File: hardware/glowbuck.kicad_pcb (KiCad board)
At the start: 4 copper layers, 80 x 50 mm, 130 parts, among them J101 Conn_02x08_Odd_Even, J102 Conn_01x04_Socket, J103 Conn_01x01_Pin, J104 Conn_01x01_Pin, J105 Conn_01x01_Pin, J201 USB_C_Receptacle_USB2.0_16P, J202 USB_C_Receptacle_USB2.0_16P, Q401 2N7002NXAKR, SW101 SW_Push, SW102 SW_Push, U101 ESP32-S3-WROOM-1, U102 INA181A3, U103 SN74LVC1T45DBV, U201 TPS25730D, U202 TPD2E2U06DCK, U301 AP63203WU, U401 SIC437A

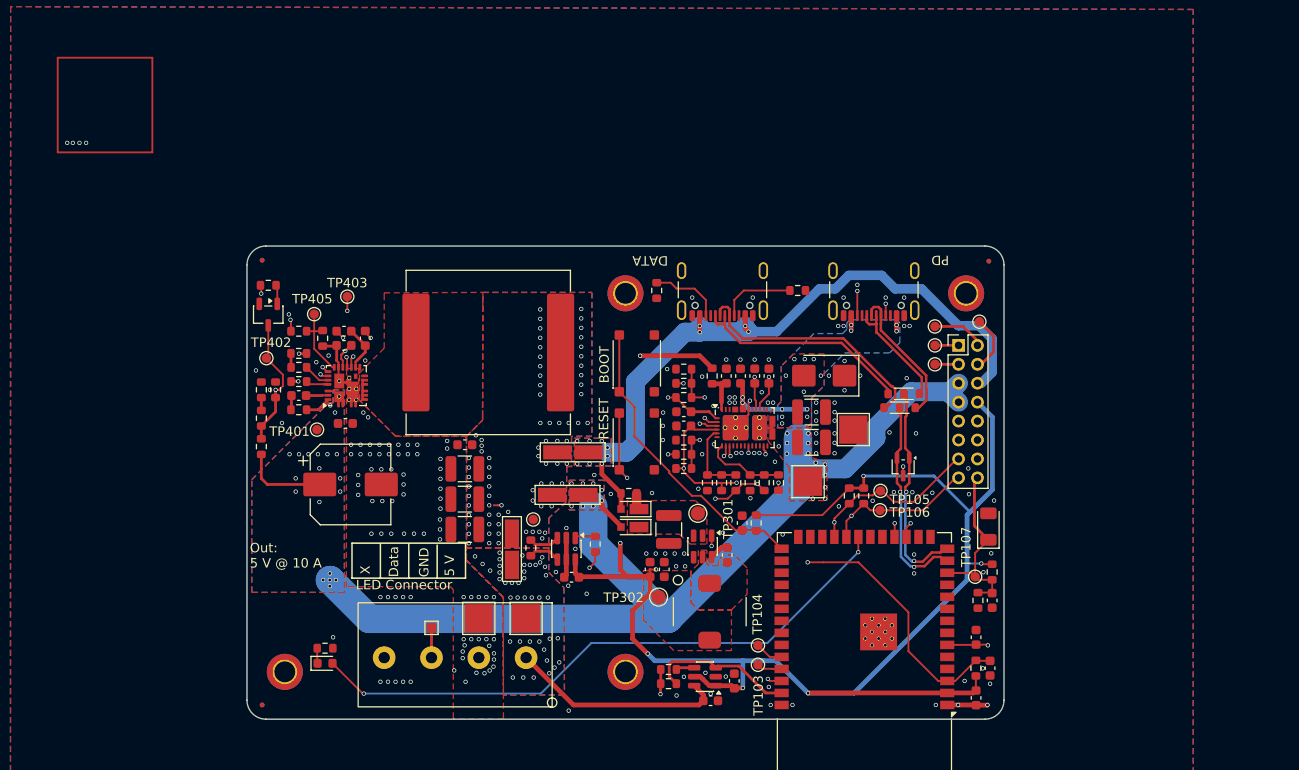
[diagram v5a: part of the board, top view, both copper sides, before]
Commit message: Exchanged shunt resistor
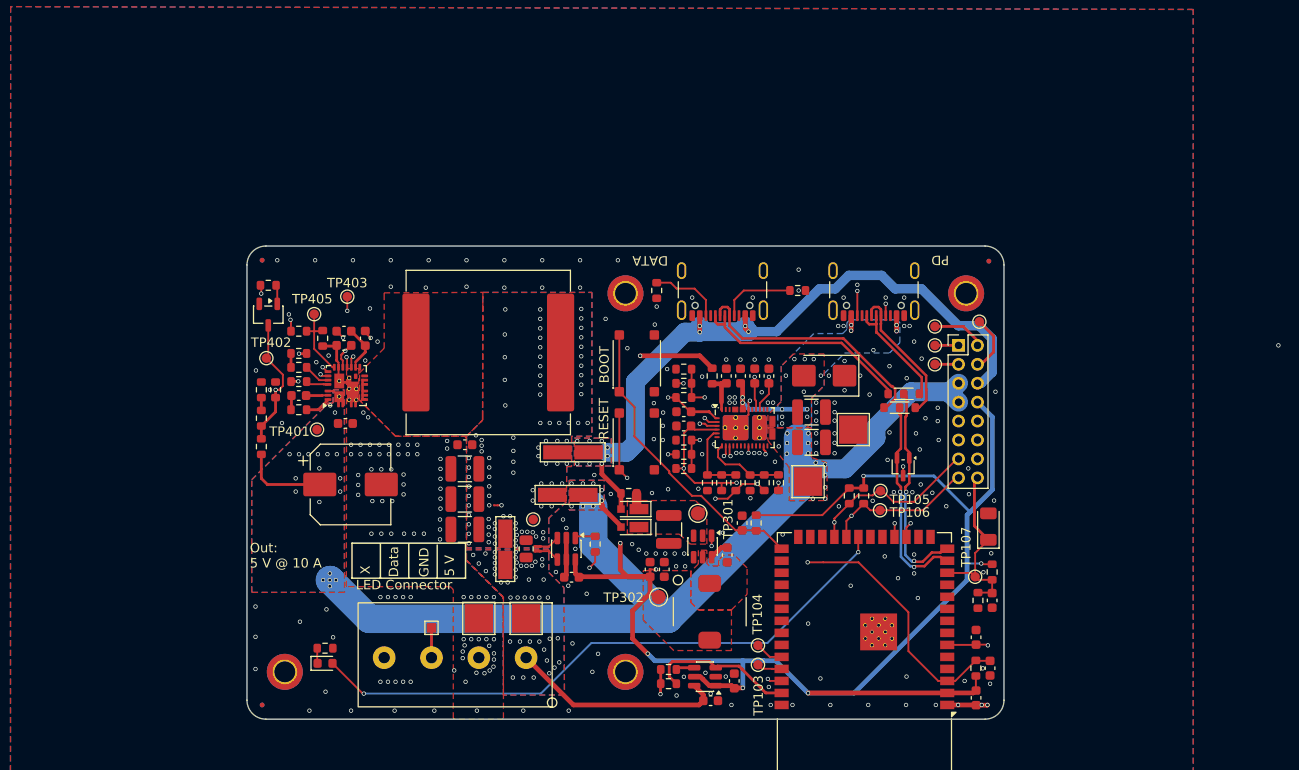
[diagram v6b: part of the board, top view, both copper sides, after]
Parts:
- R109: footprint Resistor_SMD:R_0603_1608Metric -> Resistor_SMD:R_0805_2012Metric
- moved JP103 0.70 mm to (81.3, 82.0)
- moved R109 0.51 mm to (83.5, 82.0)
- moved NT101 0.20 mm to (84.7, 81.8)
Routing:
- net VOUT: vias 75 -> 91
- net GND: vias 192 -> 263
- net /LED_POW: vias 41 -> 44
- net (no net): vias 4 -> 1

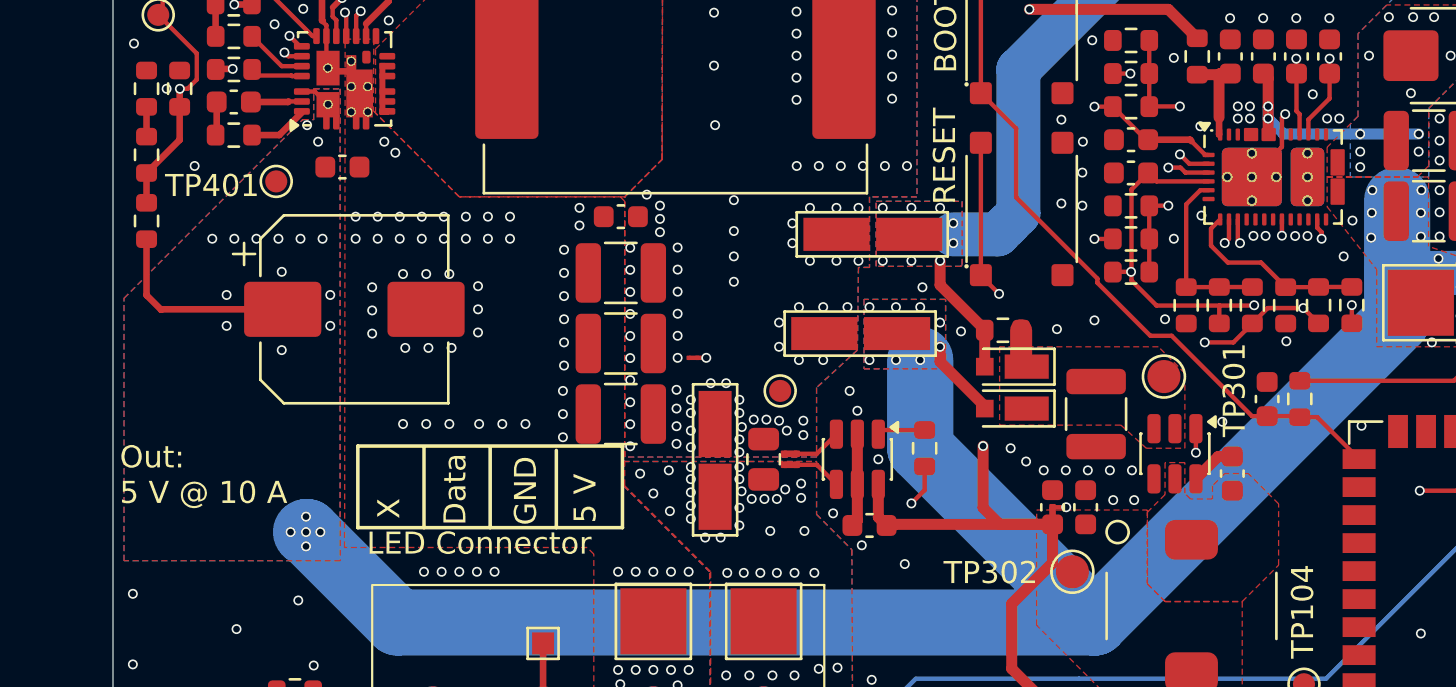
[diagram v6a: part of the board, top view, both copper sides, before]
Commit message: Added ManufacturerNumber for every item and fixed bom errors
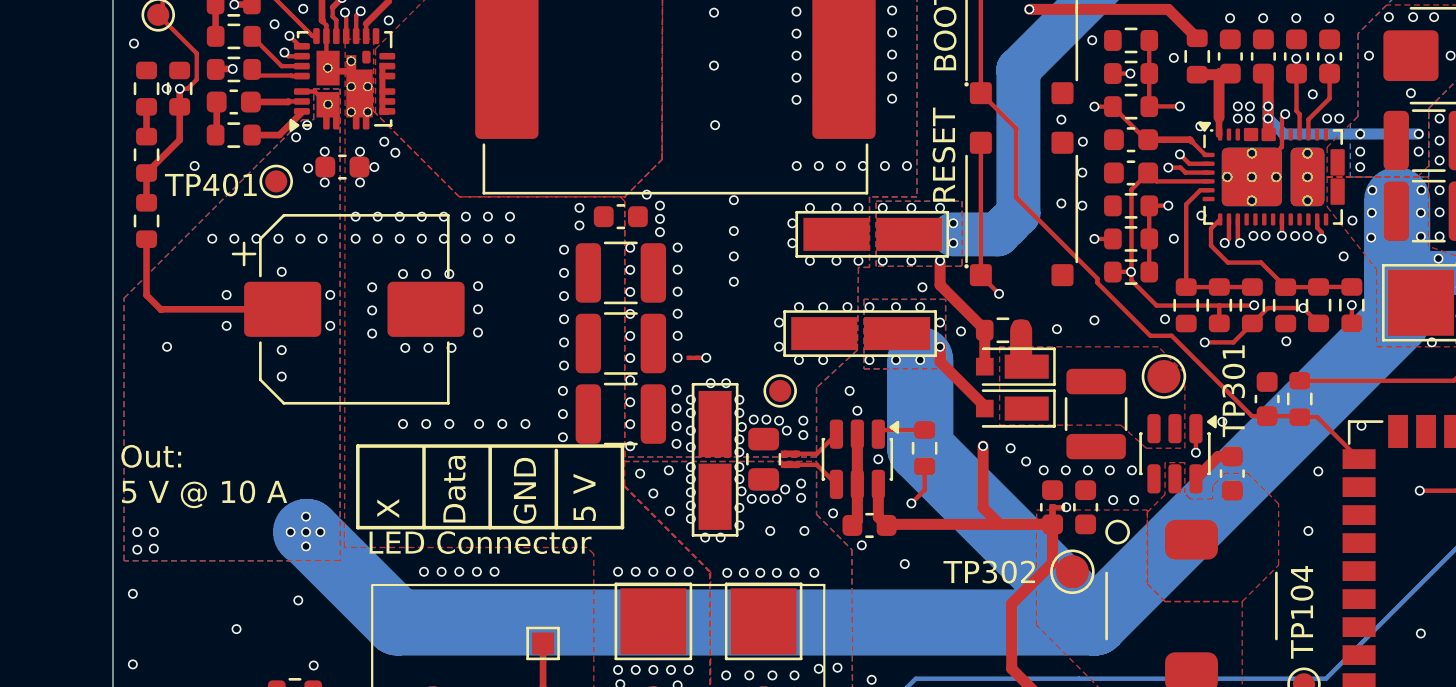
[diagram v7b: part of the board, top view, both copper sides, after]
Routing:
- net VBUS: vias 40 -> 49
- net GND: vias 263 -> 268
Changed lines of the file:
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@@
+	)
+	(via
+		(at 65.2 69.45)
+		(size 0.45)
+		(drill 0.3)
+		(layers "F.Cu" "B.Cu")
+		(free yes)
+		(net 2)
 	)
 	(via
@@
 	)
 	(via
+		(at 65.2 68.05)
+		(size 0.45)
+		(drill 0.3)
+		(layers "F.Cu" "B.Cu")
+		(free yes)
+		(net 2)
+	)
+	(via
 		(at 97.95 70.5)
 		(size 0.45)
@@
 	)
 	(via
+		(at 65.85 68.75)
+		(size 0.45)
+		(drill 0.3)
+		(layers "F.Cu" "B.Cu")
+		(free yes)
+		(net 2)
+	)
+	(via
 		(at 68.1 96.05)
 		(size 0.45)
@@
 	)
 	(via
+		(at 108.2 85.25)
+		(size 0.45)
+		(drill 0.3)
+		(layers "F.Cu" "B.Cu")
+		(free yes)
+		(net 2)
+	)
+	(via
 		(at 73.8 99.1)
 		(size 0.45)
@@
 	(via
 		(at 132.53 96.26)
+		(size 0.45)
+		(drill 0.3)
+		(layers "F.Cu" "B.Cu")
+		(free yes)
+		(net 2)
+	)
+	(via
+		(at 108.65 82.55)
 		(size 0.45)
 		(drill 0.3)
@@
 	)
 	(via
+		(at 63.6 68.05)
+		(size 0.45)
+		(drill 0.3)
+		(layers "F.Cu" "B.Cu")
+		(free yes)
+		(net 3)
+	)
+	(via
 		(at 59.15 75.95)
 		(size 0.45)
@@
 	)
 	(via
+		(at 55.1 85.3)
+		(size 0.45)
+		(drill 0.3)
+		(layers "F.Cu" "B.Cu")
+		(free yes)
+		(net 3)
+	)
+	(via
 		(at 62.800837 66.850837)
 		(size 0.45)
@@
 	)
 	(via
+		(at 61.65 78.25)
+		(size 0.45)
+		(drill 0.3)
+		(layers "F.Cu" "B.Cu")
+		(free yes)
+		(net 3)
+	)
+	(via
 		(at 59.5 72)
 		(size 0.45)
@@
 	)
 	(via
+		(at 62.85 68.8)
+		(size 0.45)
+		(drill 0.3)
+		(layers "F.Cu" "B.Cu")
+		(free yes)
+		(net 3)
+	)
+	(via
 		(at 115.1 73.1)
 		(size 0.45)
@@
 	)
 	(via
+		(at 55.85 86.05)
+		(size 0.45)
+		(drill 0.3)
+		(layers "F.Cu" "B.Cu")
+		(free yes)
+		(net 3)
+	)
+	(via
 		(at 113.3 70.825)
 		(size 0.45)
@@
 	)
 	(via
-		(at 63.3 67.6)
+		(at 62.3 67.4)
 		(size 0.45)
 		(drill 0.3)
@@
 	)
 	(via
+		(at 56.45 76.9)
+		(size 0.45)
+		(drill 0.3)
+		(layers "F.Cu" "B.Cu")
+		(free yes)
+		(net 3)
+	)
+	(via
 		(at 114.1 72.9)
 		(size 0.45)
@@
 	)
 	(via
+		(at 55.1 86.1)
+		(size 0.45)
+		(drill 0.3)
+		(layers "F.Cu" "B.Cu")
+		(free yes)
+		(net 3)
+	)
+	(via
 		(at 113.3 71.9)
 		(size 0.45)
@@
 	)
 	(via
+		(at 63.6 69.45)
+		(size 0.45)
+		(drill 0.3)
+		(layers "F.Cu" "B.Cu")
+		(free yes)
+		(net 3)
+	)
+	(via
 		(at 90.6 77.5)
 		(size 0.45)
@@
 		(net 3)
 	)
+	(via
+		(at 55.85 85.3)
+		(size 0.45)
+		(drill 0.3)
+		(layers "F.Cu" "B.Cu")
+		(free yes)
+		(net 3)
+	)

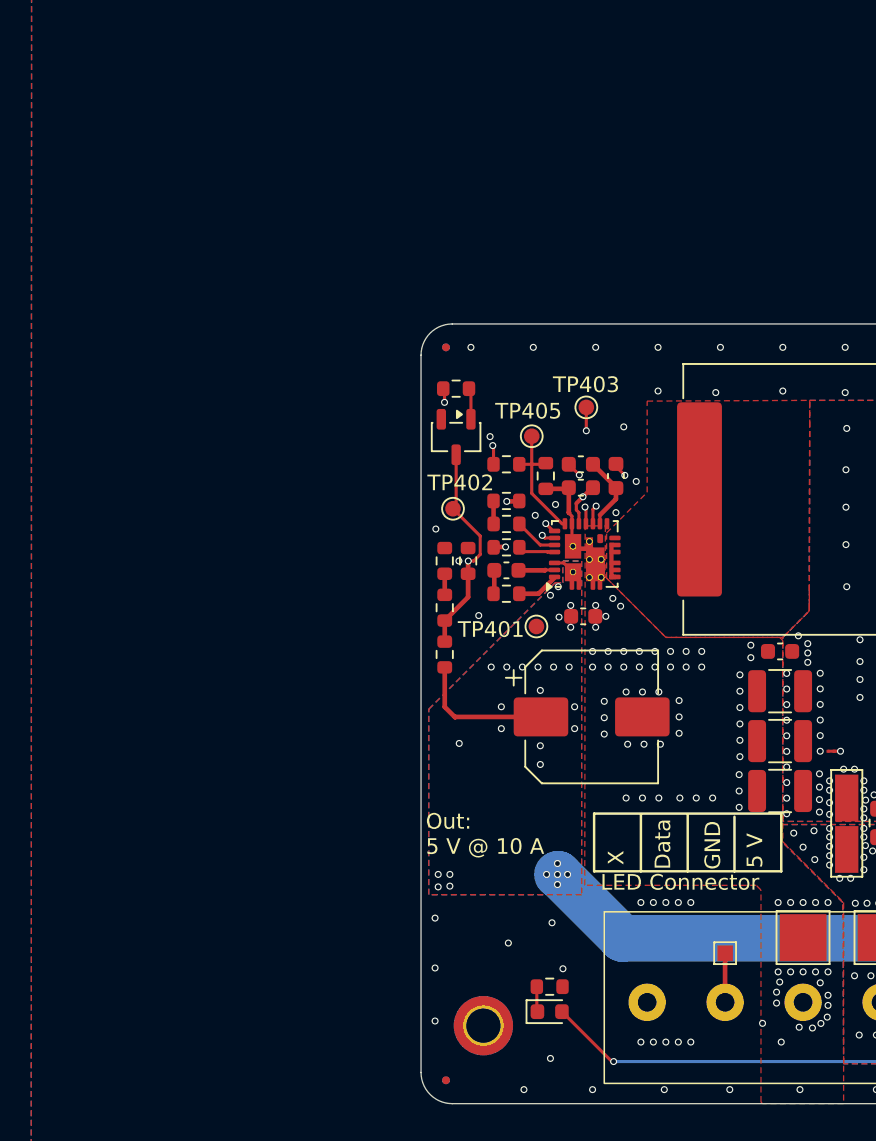
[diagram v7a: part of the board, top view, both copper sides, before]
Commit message: Connected VBUS to the free phoenix connector pin
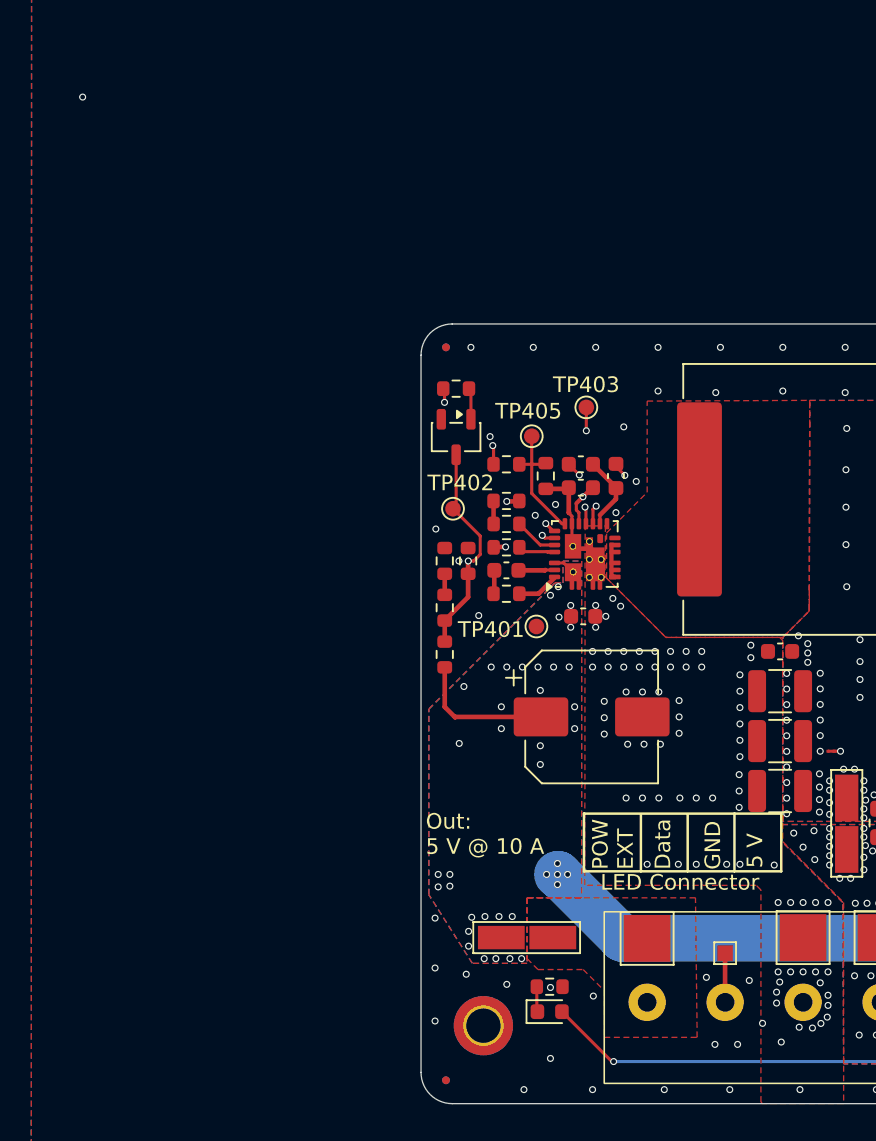
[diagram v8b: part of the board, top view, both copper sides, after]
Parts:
- added J106: Conn_01x01_Pin, TestPoint:TestPoint_Pad_3.0x3.0mm, F.Cu at (68.5, 89.4)
- added JP104: SolderJumper_2_Open, glowbuck:SolderJumper_Open_HighCurrent, F.Cu at (60.8, 89.3)
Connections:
- J102 pad 4: unconnected-(J102-Pin_4-Pad4) -> /VBUS_EXT
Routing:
- net VBUS: vias 49 -> 60
- net GND: vias 268 -> 269
- net (no net): vias 1 -> 2
- added copper zone on F.Cu, net /VBUS_EXT
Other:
- board text added: "POW EXT"
- board text removed: "X"
